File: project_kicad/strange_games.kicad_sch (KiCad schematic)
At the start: 123 parts, among them J1 Display, M1 Motor_DC, Q1 Si2302A, Q3 Si2302A, Q4 Q_Photo, SW1 SW_Push, SW10 SW_Push, SW11 SW_Push, SW12 SW_Push, SW2 SW_Push, SW3 SW_Push, SW4 SW_Push, SW5 SW_Push, SW6 SW_Push, SW7 SW_Push, SW8 SW_Push, SW9 SW_Push, U1 charge controller, U2 boost converter, U3 LDL1117S33R, U4 ESP32-DEVKIT-V1, U5 TMP112xxDRL, U6 vibrating_sensor, U7 LSM6DS3, U8 MQ-135 gas sensor

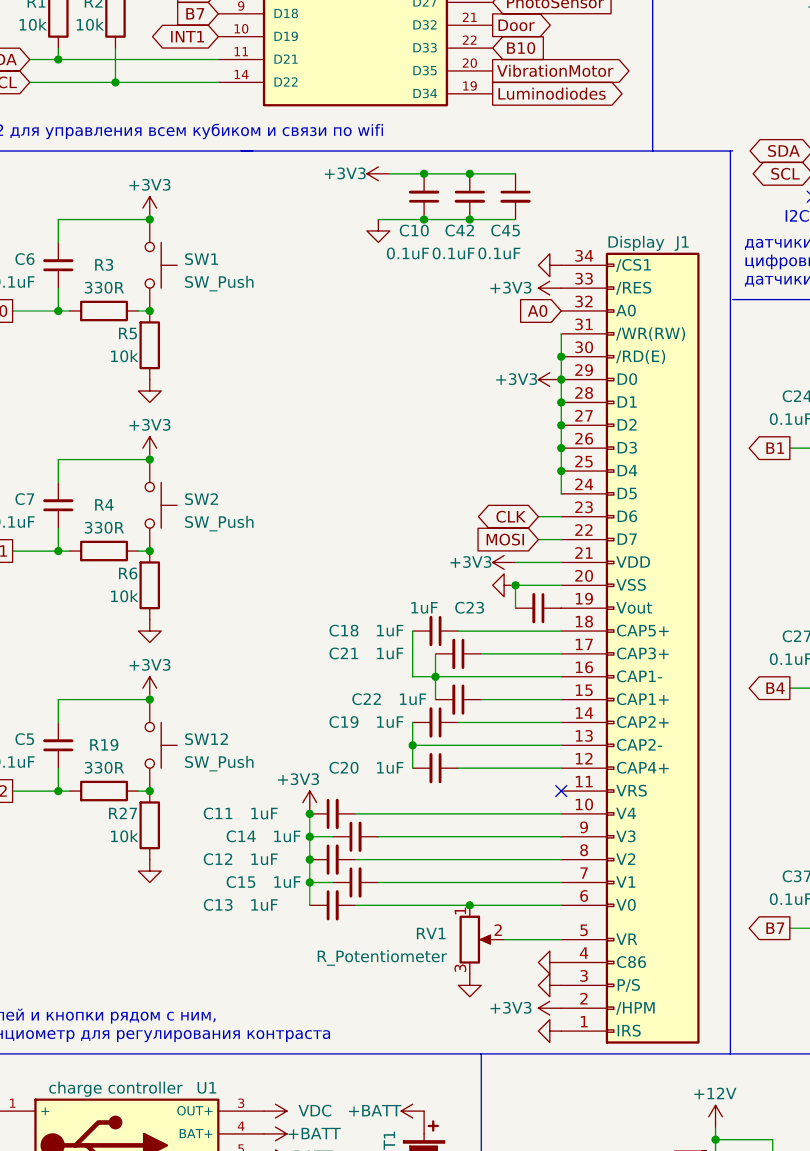
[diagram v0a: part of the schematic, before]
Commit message: code update and pcb remade a0 track
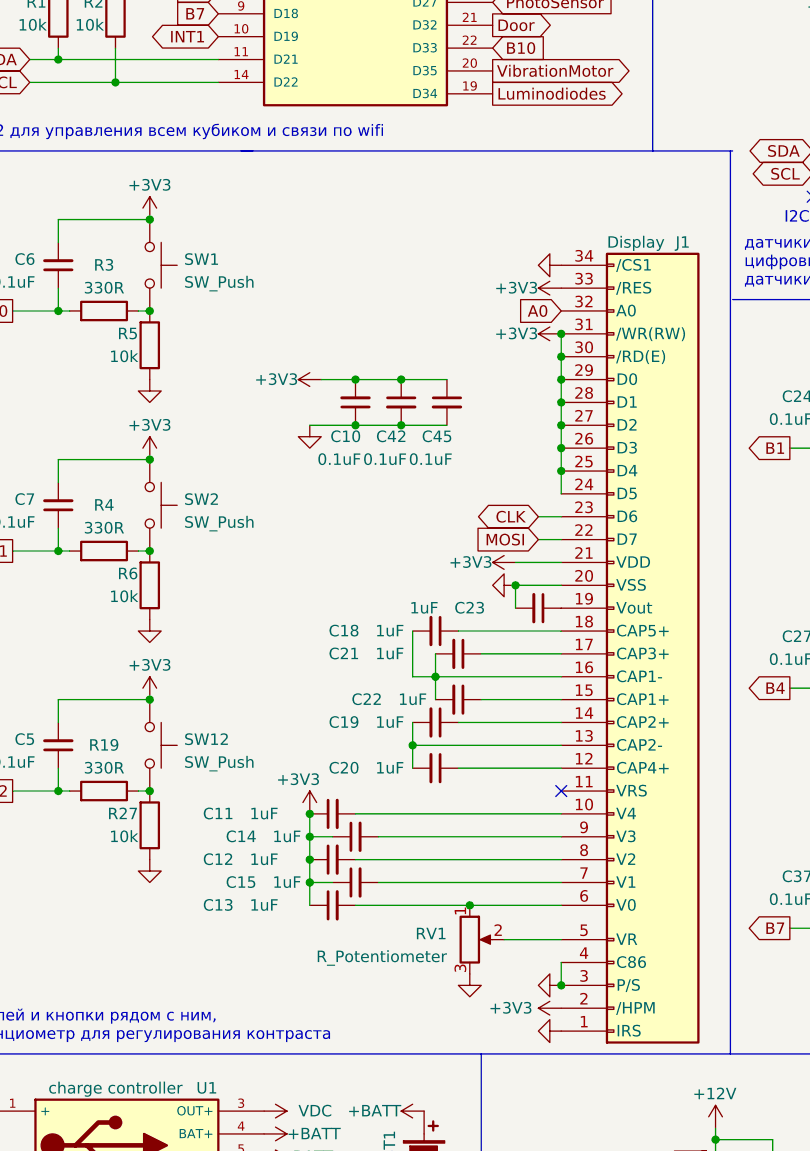
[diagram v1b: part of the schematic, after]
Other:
- moved on the sheet: C10, C42, C45

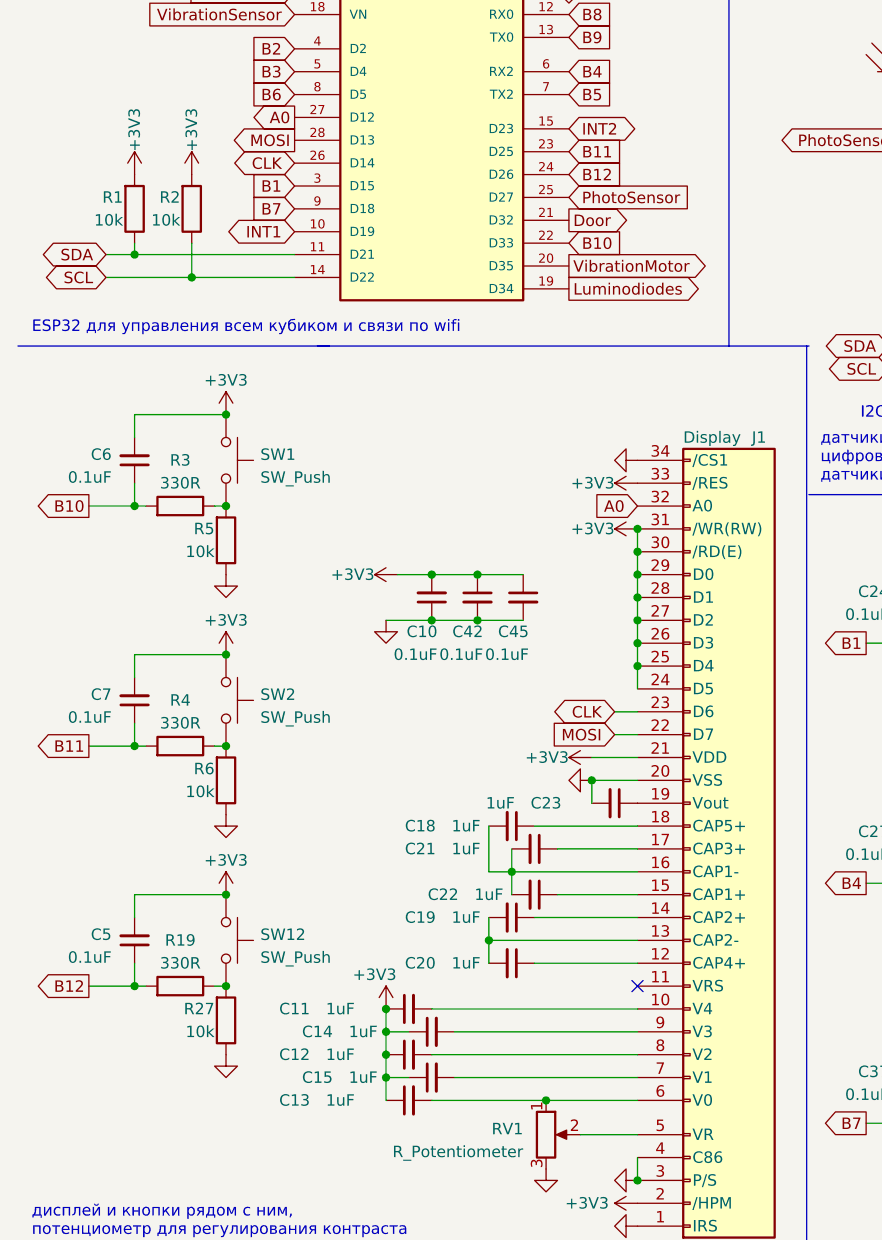
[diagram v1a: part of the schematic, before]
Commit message: pcb changes deleted 1 button and made /res pin
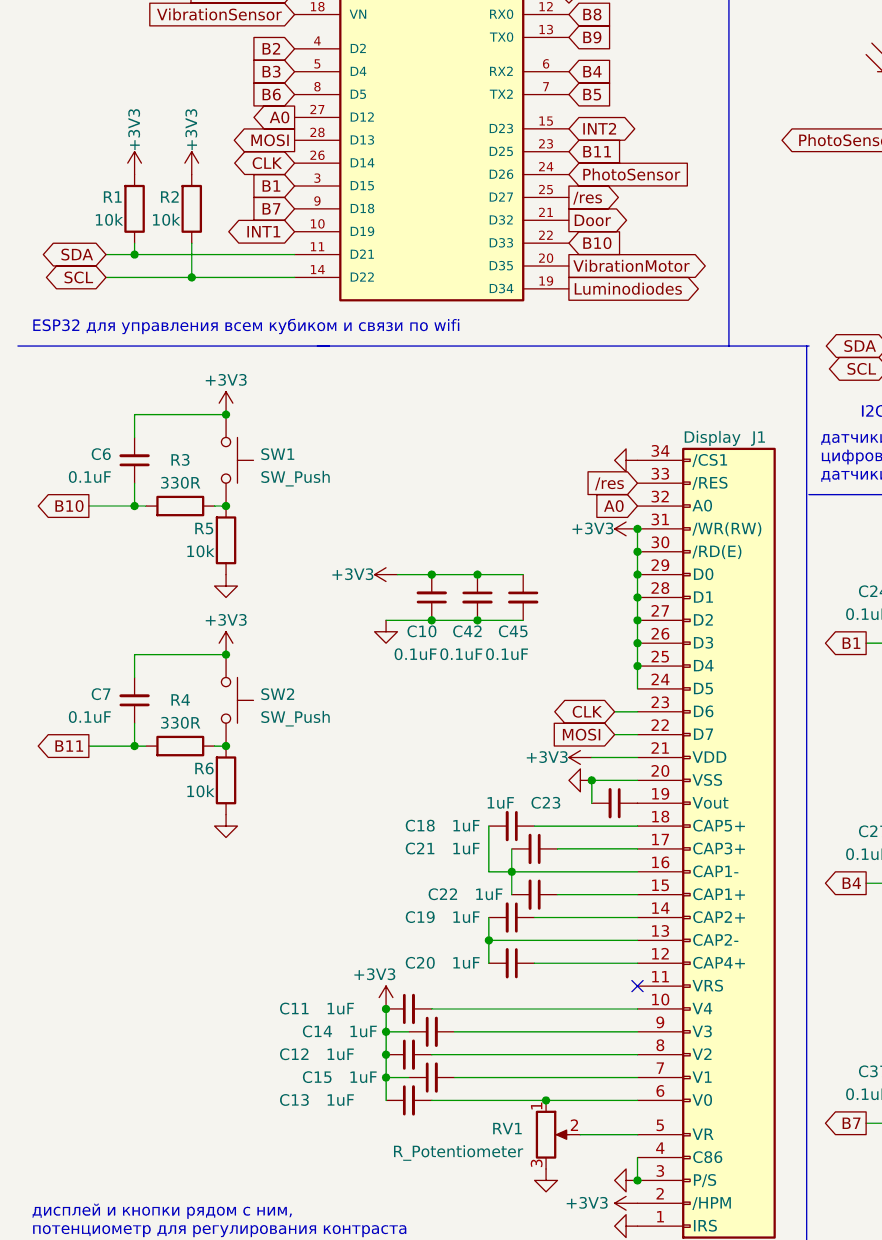
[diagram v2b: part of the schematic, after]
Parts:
- removed C5: C_Generic, PCM_Capacitor_SMD_AKL:C_0402_1005Metric, symbol Library:C_Generic
- removed R19: 330_0805, PCM_4ms_Resistor:R_0805_2012Metric, symbol Library:1.2k_0603
- removed R27: 10k_0805, PCM_4ms_Resistor:R_0805_2012Metric, symbol Library:1.2k_0603
- removed SW12: SW_Push, Button_Switch_THT:SW_PUSH-12mm, symbol Switch:SW_Push
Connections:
- net B12 is gone; now on net PhotoSensor: U4.24 (D26)
- net +3V3: no longer J1.33 (/RES)
- net PhotoSensor: no longer U4.25 (D27)
- new net /res: J1.33 (/RES), U4.25 (D27)

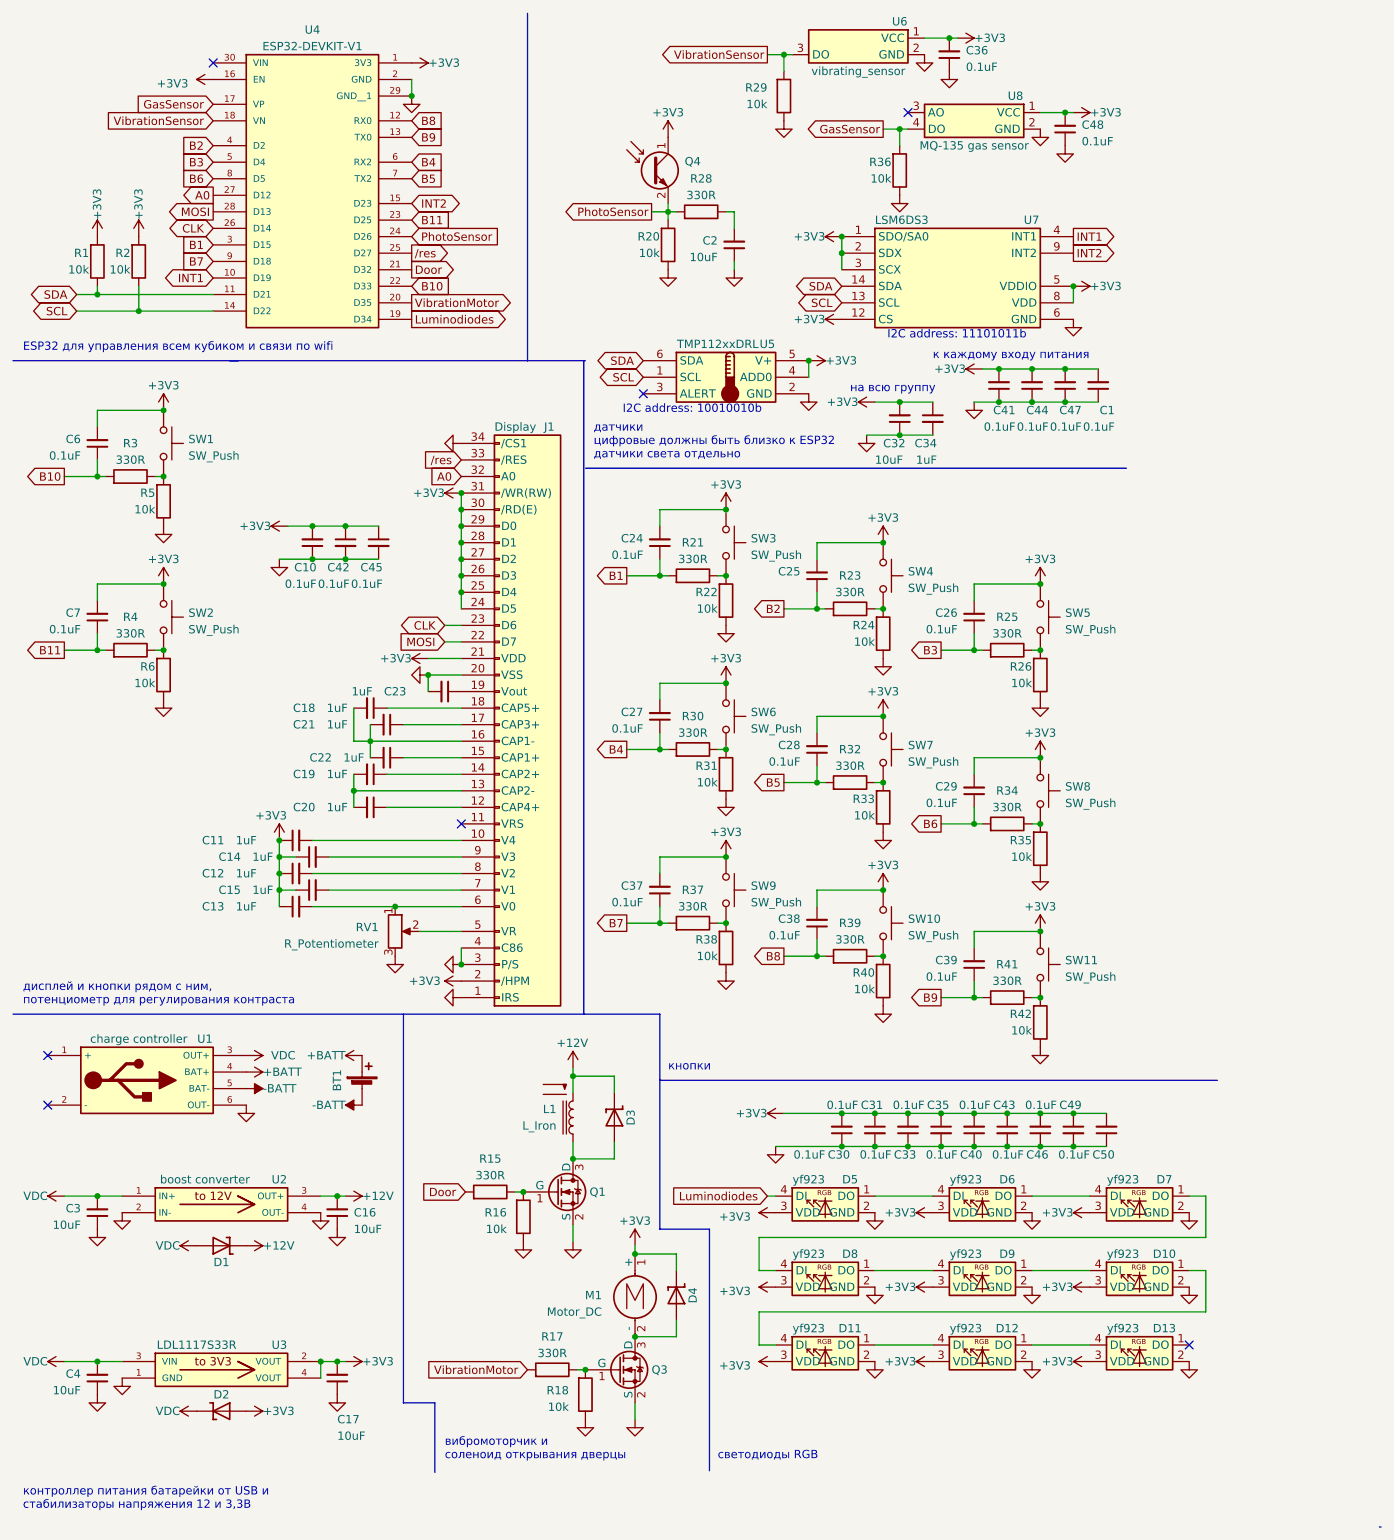
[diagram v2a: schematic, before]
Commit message: pcb changes
Remade traces: now the are 1mm wide
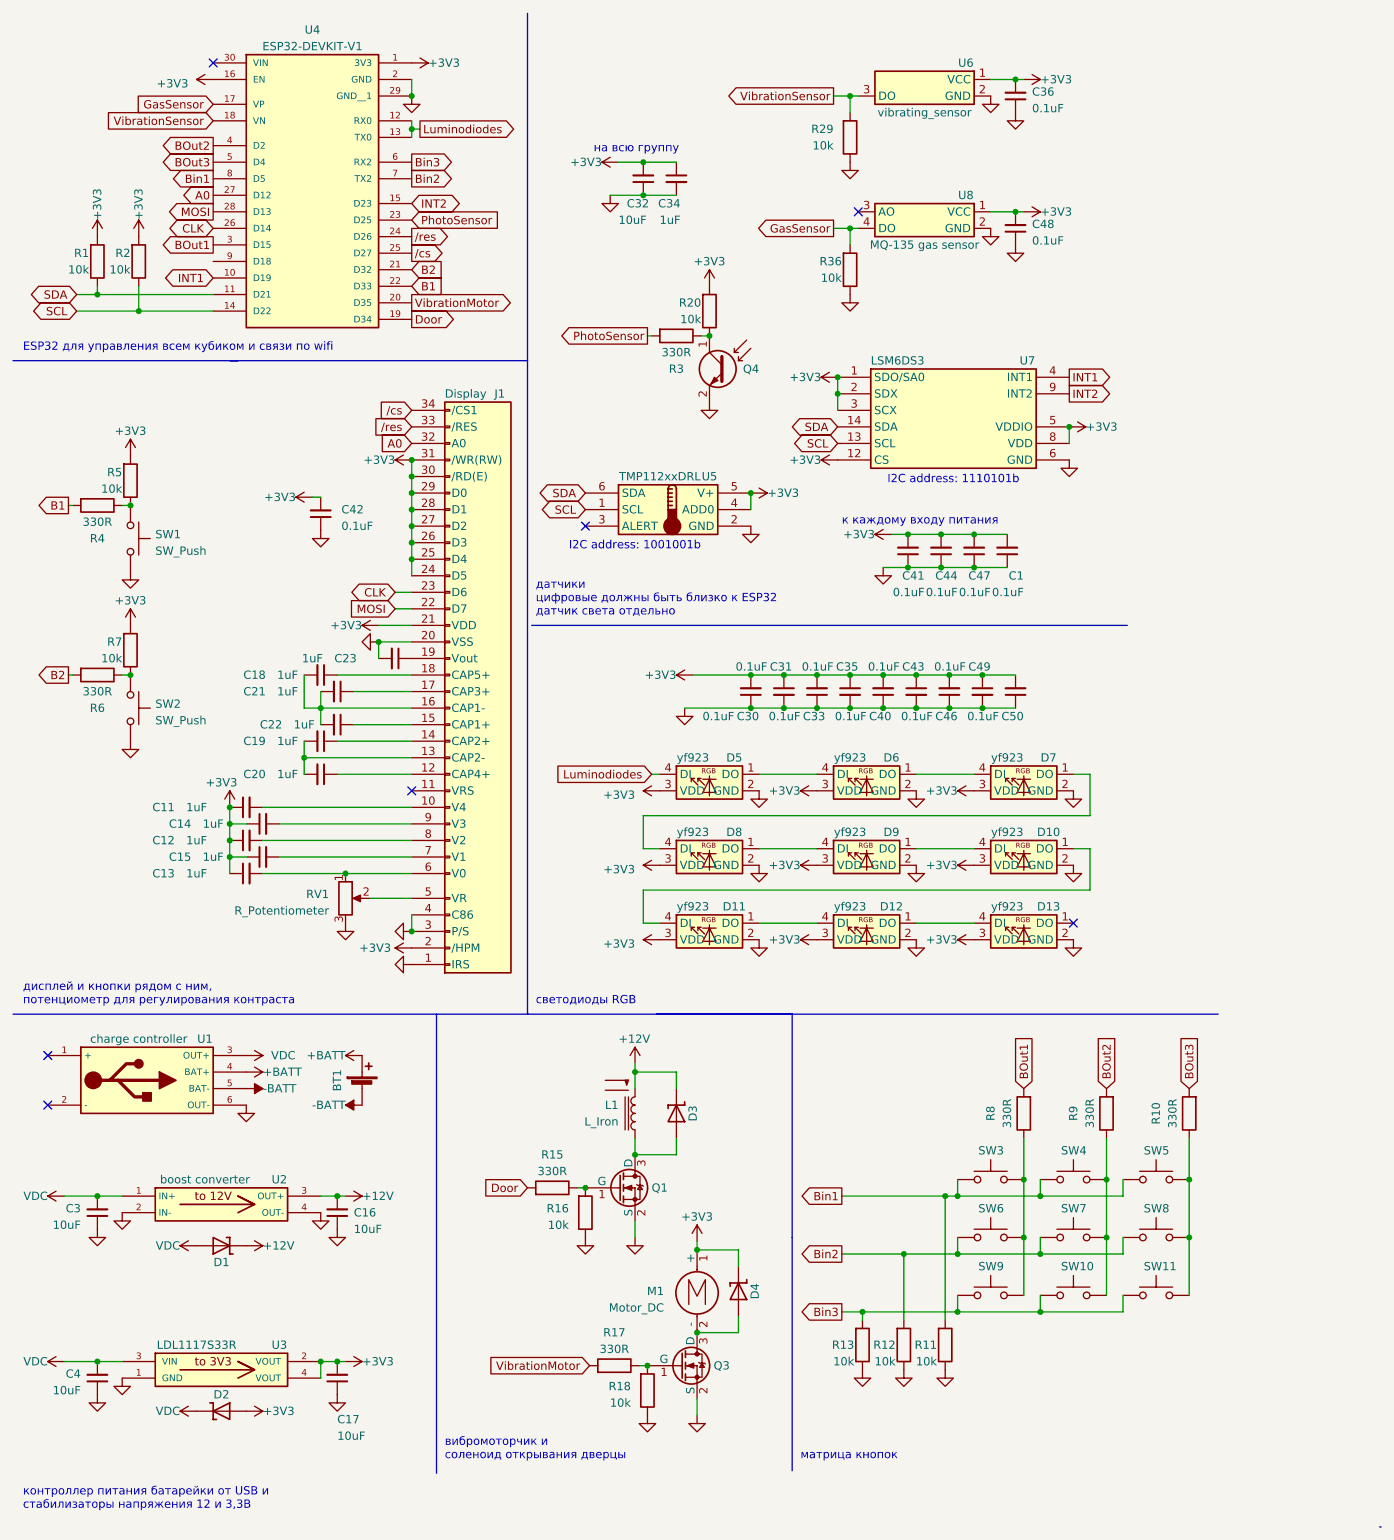
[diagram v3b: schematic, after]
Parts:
- removed C2: C_Generic, PCM_Capacitor_SMD_AKL:C_0805_2012Metric, symbol Library:C_Generic
- removed C24, C25, C26, C27, C28, C29, C37, C38, C39, C42, C45, C6, C7: C_Generic, PCM_Capacitor_SMD_AKL:C_0402_1005Metric, symbol Library:C_Generic
- removed R21, R23, R25, R28, R30, R32, R34, R37, R39, R41: 330_0805, PCM_4ms_Resistor:R_0805_2012Metric, symbol Library:1.2k_0603
- removed R22, R24, R26, R31, R33, R35, R38, R40, R42: 10k_0805, PCM_4ms_Resistor:R_0805_2012Metric, symbol Library:1.2k_0603
- added R10, R8, R9: 330_0805, PCM_4ms_Resistor:R_0805_2012Metric, symbol Library:1.2k_0603
- added R11, R12, R13, R7: 10k_0805, PCM_4ms_Resistor:R_0805_2012Metric, symbol Library:1.2k_0603
- R6: value 10k_0805 -> 330_0805; Display 10k -> 330R; Specifications 10K, 1%, 1/10W, 0805 -> 330, 1%, 1/10W, 0805
- renumbered C10 to C42
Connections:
- net B8 is gone; now on net Luminodiodes: U4.12 (RX0)
- net B9 is gone; now on net Luminodiodes: U4.13 (TX0)
- net +3V3: now also R20.2, R5.2, R7.2; no longer Q4.1 (C), SW1.1, SW10.1, SW11.1, SW2.1, SW3.1, SW4.1, SW5.1, SW6.1, SW7.1, SW8.1, SW9.1
- net B1: now also R4.2, U4.22 (D33); no longer U4.3 (D15)
- net B2: now also R6.2, U4.21 (D32); no longer U4.4 (D2)
- net Door: now also U4.19 (D34); no longer U4.21 (D32)
- net GND: now also Q4.2 (E), SW1.2, SW2.2, R11.1, R12.1, R13.1; no longer J1.34 (/CS1), R20.1, R5.1, R6.1
- net Luminodiodes: no longer U4.19 (D34)
- net PhotoSensor: now also R3.2, U4.23 (D25); no longer Q4.2 (E), R20.2, U4.24 (D26)
- net /res: now also U4.24 (D26); no longer U4.25 (D27)
- net at SW6.2: now also SW3.2, SW9.2, R8.1
- net at SW7.2: now also SW10.2, SW4.2, R9.1
- net at SW11.2: now also SW5.2, SW8.2, R10.1
- removed net B10: R3.2, U4.22 (D33)
- removed net B11: R4.2, U4.23 (D25)
- net B3 renamed BOut3
- net BOut3: now also R10.2
- net B4 renamed Bin3
- net Bin3: now also SW10.1, SW11.1, SW9.1, R13.2
- net B5 renamed Bin2
- net Bin2: now also SW6.1, SW7.1, SW8.1, R12.2
- net B6 renamed Bin1
- net Bin1: now also SW3.1, SW4.1, SW5.1, R11.2
- net B7: no longer names the net of U4.9 (D18)
- new net: R4.1, R5.1, SW1.1
- new net: R6.1, R7.1, SW2.1
- new net: Q4.1 (C), R20.1, R3.1
- new net BOut1: R8.2, U4.3 (D15)
- new net BOut2: R9.2, U4.4 (D2)
- new net /cs: J1.34 (/CS1), U4.25 (D27)
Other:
- note added: "I2C address: 1001001b"
- note added: "I2C address: 1110101b"
- note added: "датчики цифровые должны быть близко к ESP32 датчик света отдельно"
- note added: "матрица кнопок"
- note removed: "I2C address: 10010010b"
- note removed: "I2C address: 11101011b"
- note removed: "датчики цифровые должны быть близко к ESP32 датчики света отдельно"
- note removed: "кнопки"
- moved on the sheet: C1, C11, C12, C13, C14, C15, C18, C19, C20, C21, C22, C23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

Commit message: I need to remaster everything
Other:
- moved on the sheet: C11, C12, C13, C14, C15, C18, C19, C20, C21, C22, C23, C42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
